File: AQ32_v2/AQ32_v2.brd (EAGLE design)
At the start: 57.1 x 57.1 mm, 116 parts, among them Q2 BCV27, Q3 BCV27, Q5 BCV27, Q6 BCV27, U1 ITG-3200, U10 MS5611, U11 MIC5239, U13 74AHC1G86DCK, U2 STM32F10XVXT6, U7 USD-SOCKETNEW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

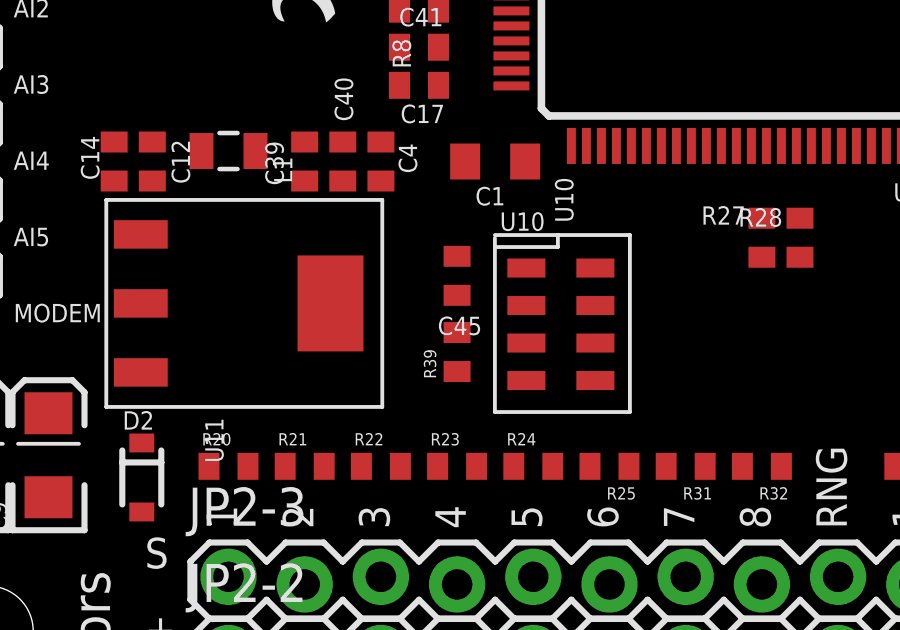
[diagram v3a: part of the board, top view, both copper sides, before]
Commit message: converted baro back to using I2C, renamed TX4/TX5 to use I2C3 labels
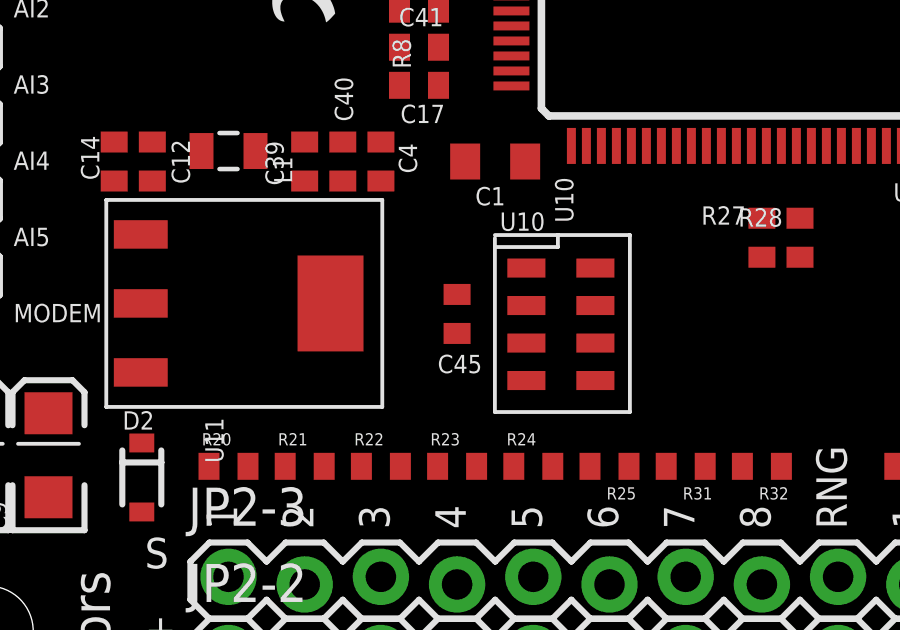
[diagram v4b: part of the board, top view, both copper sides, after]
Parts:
- removed R39: 10K, SparkFun:C0402
- moved C45 1.27 mm to (21.6, 16.5)
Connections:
- net UART4_TX renamed SCK3_LV
- net UART5_TX renamed MOSI3_LV
- removed net BARO_CS: R39.1, U10.4, U10.5, U2.57
- removed net BARO_PS: U10.2, U2.38
- removed net UART4_RX: R48.2, U1.9, U10.6, U2.79
- new net MISO3_LV: R48.2, U1.9, U2.79
- new net PD10: U2.57
- new net PE7: U2.38
- net 3V3DIG: now also U10.2, U10.4, U10.5; no longer R39.2
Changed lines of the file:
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@@
 <attribute name="NAME" x="24.8572" y="21.061" size="0.6096" layer="25" rot="R270"/>
 </element>
-<element name="C45" library="rcl" package="C0402" value="0.1uF" x="21.59" y="17.78" smashed="yes" rot="R270">
-<attribute name="NAME" x="22.4236" y="16.4162" size="0.6096" layer="25" rot="R180"/>
-<attribute name="VALUE" x="19.685" y="18.415" size="1.27" layer="27" rot="R270"/>
+<element name="C45" library="rcl" package="C0402" value="0.1uF" x="21.59" y="16.51" smashed="yes" rot="R270">
+<attribute name="NAME" x="22.4236" y="15.1462" size="0.6096" layer="25" rot="R180"/>
+<attribute name="VALUE" x="19.685" y="17.145" size="1.27" layer="27" rot="R270"/>
 </element>
 <element name="U11" library="DSP-TI" package="TO-223" value="MIC5239" x="11.06" y="16.86" smashed="yes" rot="R270">
@@
 <element name="JP3-1" library="SparkFun-Connectors" package="1X09" value="M09" x="2.54" y="38.1" rot="R270"/>
 <element name="JP3-2" library="SparkFun-Connectors" package="1X09" value="M09" x="5.08" y="38.1" rot="R270"/>
-<element name="R39" library="SparkFun" package="C0402" value="10K" x="21.59" y="15.24" rot="R90"/>
 <element name="JP5" library="SparkFun-Connectors" package="1X02" value="" x="45.72" y="11.43"/>
 </elements>
@@
 <contactref element="GPS" pad="4"/>
 <contactref element="L2" pad="1"/>
-<contactref element="R39" pad="2"/>
+<contactref element="U10" pad="5"/>
+<contactref element="U10" pad="4"/>
+<contactref element="U10" pad="2"/>
 <wire x1="35.24" y1="52.07" x2="35.69" y2="54.61" width="0" layer="19" extent="1-1"/>
 <wire x1="33.39" y1="46.99" x2="35.24" y2="52.07" width="0" layer="19" extent="1-1"/>
@@
 <wire x1="33.02" y1="18.4" x2="37.4" y2="22.11" width="0" layer="19" extent="1-1"/>
 <wire x1="31.75" y1="18.4" x2="33.02" y2="18.4" width="0" layer="19" extent="1-1"/>
-<wire x1="51.635" y1="14.47" x2="47.64" y2="20.32" width="0" layer="19" extent="1-1"/>
-<wire x1="23.9" y1="18.04" x2="31.75" y2="18.4" width="0" layer="19" extent="1-1"/>
-<wire x1="21.59" y1="18.43" x2="23.9" y2="18.04" width="0" layer="19" extent="1-1"/>
-<wire x1="21.59" y1="15.89" x2="21.59" y2="18.43" width="0" layer="19" extent="1-1"/>
+<wire x1="26.2" y1="14.29" x2="31.75" y2="18.4" width="0" layer="19" extent="1-1"/>
+<wire x1="23.9" y1="14.29" x2="26.2" y2="14.29" width="0" layer="19" extent="1-1"/>
+<wire x1="23.9" y1="16.79" x2="23.9" y2="14.29" width="0" layer="19" extent="1-1"/>
+<wire x1="23.9" y1="18.04" x2="23.9" y2="16.79" width="0" layer="19" extent="1-1"/>
+<wire x1="21.59" y1="17.16" x2="23.9" y2="18.04" width="0" layer="19" extent="1-1"/>
 <wire x1="23.86" y1="21.59" x2="23.9" y2="18.04" width="0" layer="19" extent="1-1"/>
 <wire x1="23.4" y1="24.11" x2="23.86" y2="21.59" width="0" layer="19" extent="1-1"/>
@@
 <wire x1="16.51" y1="22.24" x2="17.78" y2="22.24" width="0" layer="19" extent="1-1"/>
 <wire x1="14.87" y1="21.94" x2="16.51" y2="22.24" width="0" layer="19" extent="1-1"/>
+<wire x1="51.635" y1="14.47" x2="47.64" y2="20.32" width="0" layer="19" extent="1-1"/>
 <wire x1="27.94" y1="41.29" x2="33.39" y2="46.99" width="0" layer="19" extent="1-1"/>
 <wire x1="26.67" y1="41.29" x2="27.94" y2="41.29" width="0" layer="19" extent="1-1"/>
@@
 <wire x1="5.08" y1="35.56" x2="21.17" y2="37.45" width="0" layer="19" extent="1-1"/>
 </signal>
-<signal name="UART4_TX">
+<signal name="SCK3_LV">
 <contactref element="U2" pad="78"/>
 <contactref element="U1" pad="23"/>
@@
 <wire x1="26.4" y1="22.11" x2="39.91" y2="17.03" width="0" layer="19" extent="1-1"/>
 </signal>
-<signal name="UART4_RX">
+<signal name="MISO3_LV">
 <contactref element="U2" pad="79"/>
 <contactref element="U1" pad="9"/>
 <contactref element="R48" pad="2"/>
-<contactref element="U10" pad="6"/>
 <wire x1="43.91" y1="17.53" x2="46.34" y2="21.59" width="0" layer="19" extent="1-1"/>
 <wire x1="26.9" y1="22.11" x2="43.91" y2="17.53" width="0" layer="19" extent="1-1"/>
-<wire x1="26.2" y1="15.54" x2="26.9" y2="22.11" width="0" layer="19" extent="1-1"/>
 </signal>
 <signal name="TIM1_CH1">
@@
 <contactref element="U2" pad="81"/>
 </signal>
-<signal name="UART5_TX">
+<signal name="MOSI3_LV">
 <contactref element="U2" pad="80"/>
 <contactref element="U1" pad="24"/>
@@
 <wire x1="23.4" y1="32.61" x2="39.37" y2="42.53" width="0" layer="19" extent="1-1"/>
 </signal>
-<signal name="BARO_CS">
+<signal name="PD10">
 <contactref element="U2" pad="57"/>
-<contactref element="U10" pad="5"/>
-<contactref element="R39" pad="1"/>
-<contactref element="U10" pad="4"/>
-<wire x1="21.59" y1="14.59" x2="23.4" y2="33.11" width="0" layer="19" extent="1-1"/>
-<wire x1="23.9" y1="14.29" x2="21.59" y2="14.59" width="0" layer="19" extent="1-1"/>
-<wire x1="26.2" y1="14.29" x2="23.9" y2="14.29" width="0" layer="19" extent="1-1"/>
 </signal>
 <signal name="USART2_CTS">
@@
 <wire x1="23.4" y1="24.61" x2="21.86" y2="21.59" width="0" layer="19" extent="1-1"/>
 <wire x1="17.371" y1="16.86" x2="17.78" y2="20.94" width="0" layer="19" extent="1-1"/>
-<wire x1="21.59" y1="17.13" x2="17.371" y2="16.86" width="0" layer="19" extent="1-1"/>
-<wire x1="23.9" y1="15.54" x2="21.59" y2="17.13" width="0" layer="19" extent="1-1"/>
+<wire x1="21.59" y1="15.86" x2="17.371" y2="16.86" width="0" layer="19" extent="1-1"/>
+<wire x1="23.9" y1="15.54" x2="21.59" y2="15.86" width="0" layer="19" extent="1-1"/>
 <wire x1="11.08" y1="53.097" x2="9.89" y2="44.13" width="0" layer="19" extent="1-1"/>
 <wire x1="13.97" y1="2.667" x2="7.97" y2="10.4" width="0" layer="19" extent="1-1"/>
@@
 <wire x1="21.59" y1="45.07" x2="29.9" y2="38.11" width="0" layer="19" extent="1-1"/>
 </signal>
-<signal name="BARO_PS">
+<signal name="PE7">
 <contactref element="U2" pad="38"/>
-<contactref element="U10" pad="2"/>
-<wire x1="23.9" y1="16.79" x2="31.4" y2="38.11" width="0" layer="19" extent="1-1"/>
 </signal>
 <signal name="N$10">

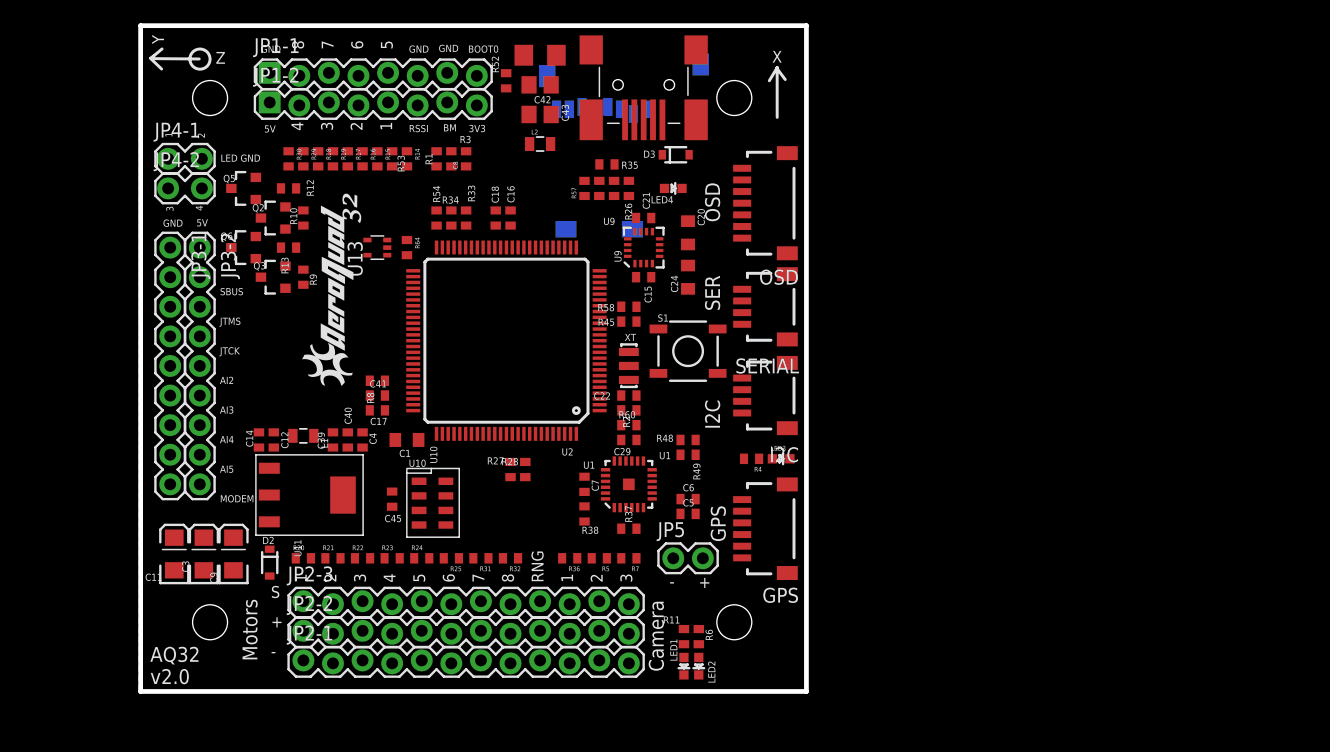
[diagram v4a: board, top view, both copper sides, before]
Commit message: fixed airwires
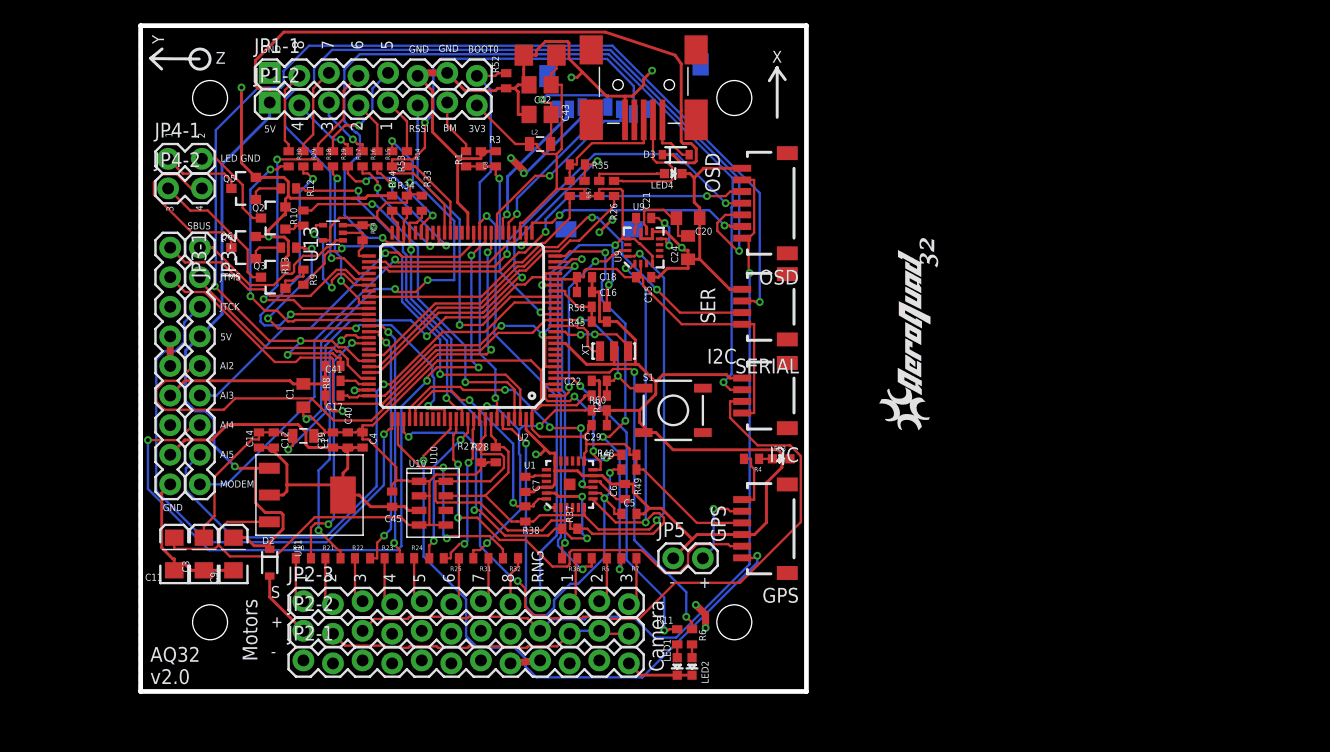
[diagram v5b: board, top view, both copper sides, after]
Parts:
- JP1-1, JP1-2: value (none) -> JP1
- JP4-1, JP4-2: value (none) -> JP4
- moved U$4 49.7 mm to (68.8, 22.4)
- moved C1 9.67 mm to (14.0, 25.4), turned to 90 degrees
- moved C18 9.16 mm to (38.1, 35.6), turned to 0 degrees
- moved C16 8.98 mm to (38.1, 34.3), turned to 0 degrees
- moved C6 5.47 mm to (41.6, 17.2), turned to 90 degrees
- moved R48 5.24 mm to (41.9, 20.3)
- moved R49 5.24 mm to (41.9, 19.1)
- moved S1 5.24 mm to (45.7, 24.1)
- moved C5 5.08 mm to (41.9, 15.2)
- moved C7 5.08 mm to (33.0, 17.8)
- moved R37 5.08 mm to (36.8, 14.0)
- moved R38 5.08 mm to (33.0, 15.2)
- moved U1 5.08 mm to (36.8, 17.8)
- moved R33 4.02 mm to (24.1, 41.9)
- moved R34 4.02 mm to (22.9, 41.9)
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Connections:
- net 5VIN: now also JP3-2.4; no longer JP3-2.1
- net GND: now also JP3-1.3; no longer JP3-1.1
- net JTAG-TRST: now also JP3-1.2; no longer JP3-1.3
- net JTCK: now also JP3-2.3; no longer JP3-2.4
- net JTMS: now also JP3-2.2; no longer JP3-2.3
- net UART3_RX: now also JP3-2.1; no longer JP3-2.2
- net UART3_TX: now also JP3-1.1; no longer JP3-1.2
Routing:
- net GND: track 0.00 -> 321.9 mm, vias 0 -> 18
- net 3V3DIG: track 0.00 -> 253.2 mm, vias 0 -> 9
- net 5VIN: track 0.00 -> 107.6 mm, vias 0 -> 1
- net UART1_RX: track 0.00 -> 103.0 mm, vias 0 -> 4
- net SCL2_LV: track 0.00 -> 82.3 mm, vias 0 -> 2
- net 3V3AN: track 0.00 -> 81.7 mm, vias 0 -> 2
- net SDA2_LV: track 0.00 -> 80.6 mm, vias 0 -> 2
- net MOSI2_LV: track 0.00 -> 76.9 mm, vias 0 -> 2
- net 5V-3: track 0.00 -> 73.0 mm, vias 0 -> 1
- net SCL1_LV: track 0.00 -> 67.9 mm, vias 0 -> 2
- net ADC12_IN15: track 0.00 -> 65.8 mm, vias 0 -> 4
- net JTAG-TRST: track 0.00 -> 56.9 mm, vias 0 -> 2
- net SDA1_LV: track 0.00 -> 54.4 mm, vias 0 -> 2
- net UART2_TX: track 0.00 -> 54.0 mm, vias 0 -> 2
- net ADC123_IN12: track 0.00 -> 50.0 mm, vias 0 -> 1
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
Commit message: fixed clearance issues
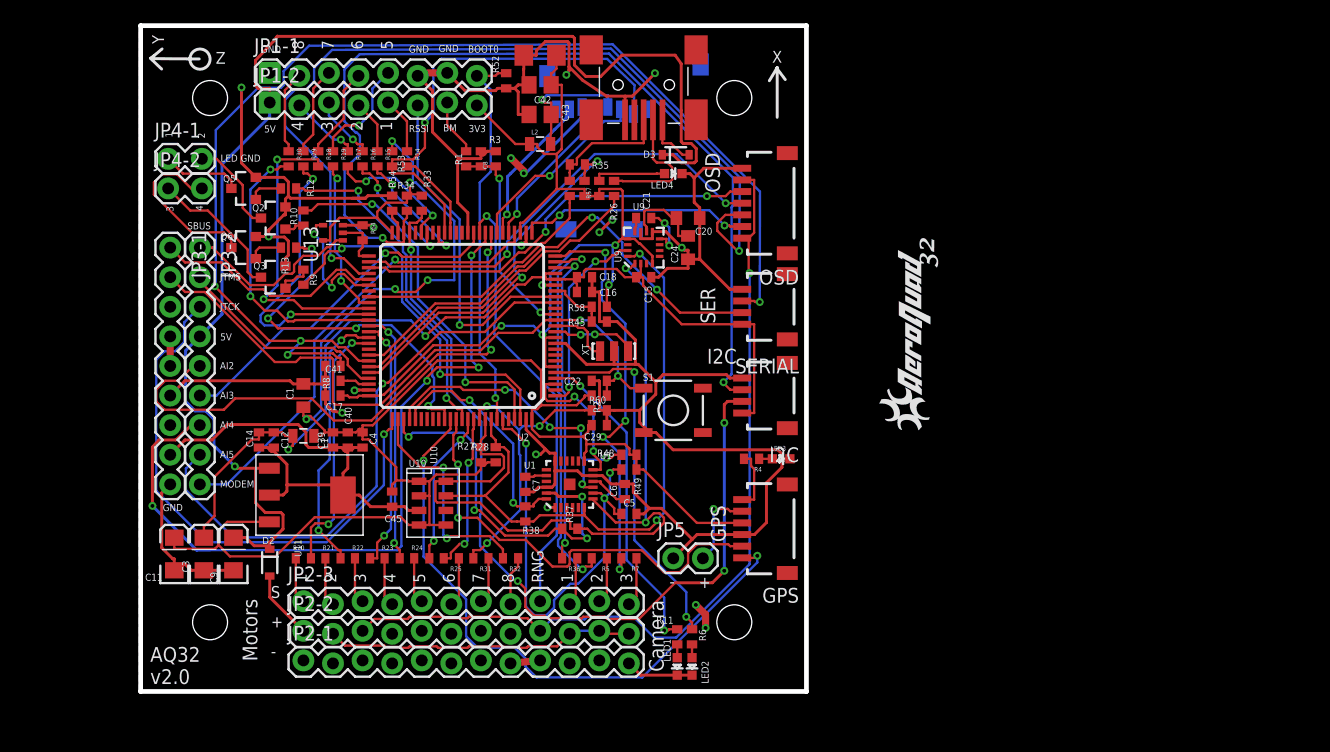
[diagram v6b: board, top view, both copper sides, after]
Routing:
- net SCL2_LV: track 82.3 -> 74.4 mm, vias 2 -> 4
- net 5VIN: track 107.6 -> 111.1 mm
